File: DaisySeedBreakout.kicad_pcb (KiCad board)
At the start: 2 copper layers, 56.4 x 76.7 mm, 173 parts, among them J10 Conn_01x03, J11 Conn_01x03, J12 Conn_01x03, J13 Conn_01x03, J14 Conn_01x03, J15 Conn_02x08, J16 Conn_01x06, J17 Conn_01x03, J19 Conn_01x03, J2 Conn_02x08, J20 Conn_01x03, J21 Conn_01x03, J22 Conn_01x03, J3 Conn_01x06, J36 MJ-3523-SMT-TR, J37 MJ-3523-SMT-TR, J38 MJ-3523-SMT-TR, J39 MJ-3523-SMT-TR, J4 5027740891, J40 MJ-3523-SMT-TR, J41 MJ-3523-SMT-TR, J42 MJ-3523-SMT-TR, J43 MJ-3523-SMT-TR, J44 MJ-3523-SMT-TR, J45 MJ-3523-SMT-TR, J5 Conn_02x08, J6 Conn_01x03, J7 Conn_01x06, J8 Conn_01x03, J9 Conn_01x03, U1 TCA6424ARGJR, U2 H11L1M, U5 MAX9814

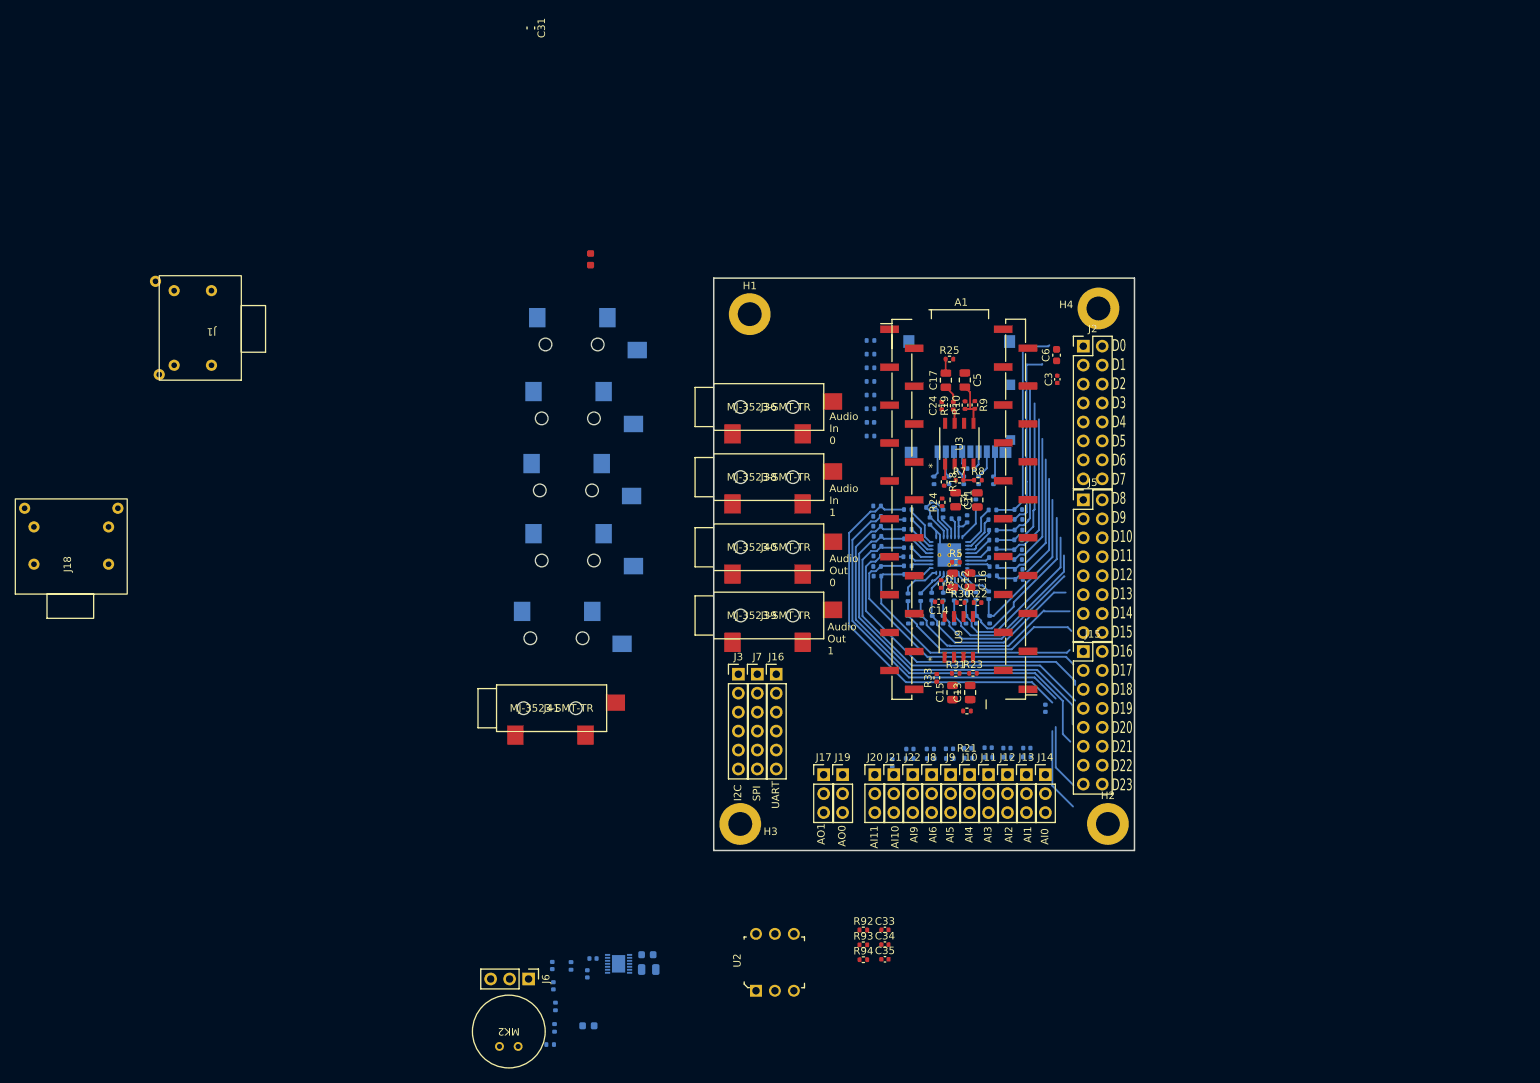
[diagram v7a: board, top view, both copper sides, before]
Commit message: added dual audio back in to prototype that concept
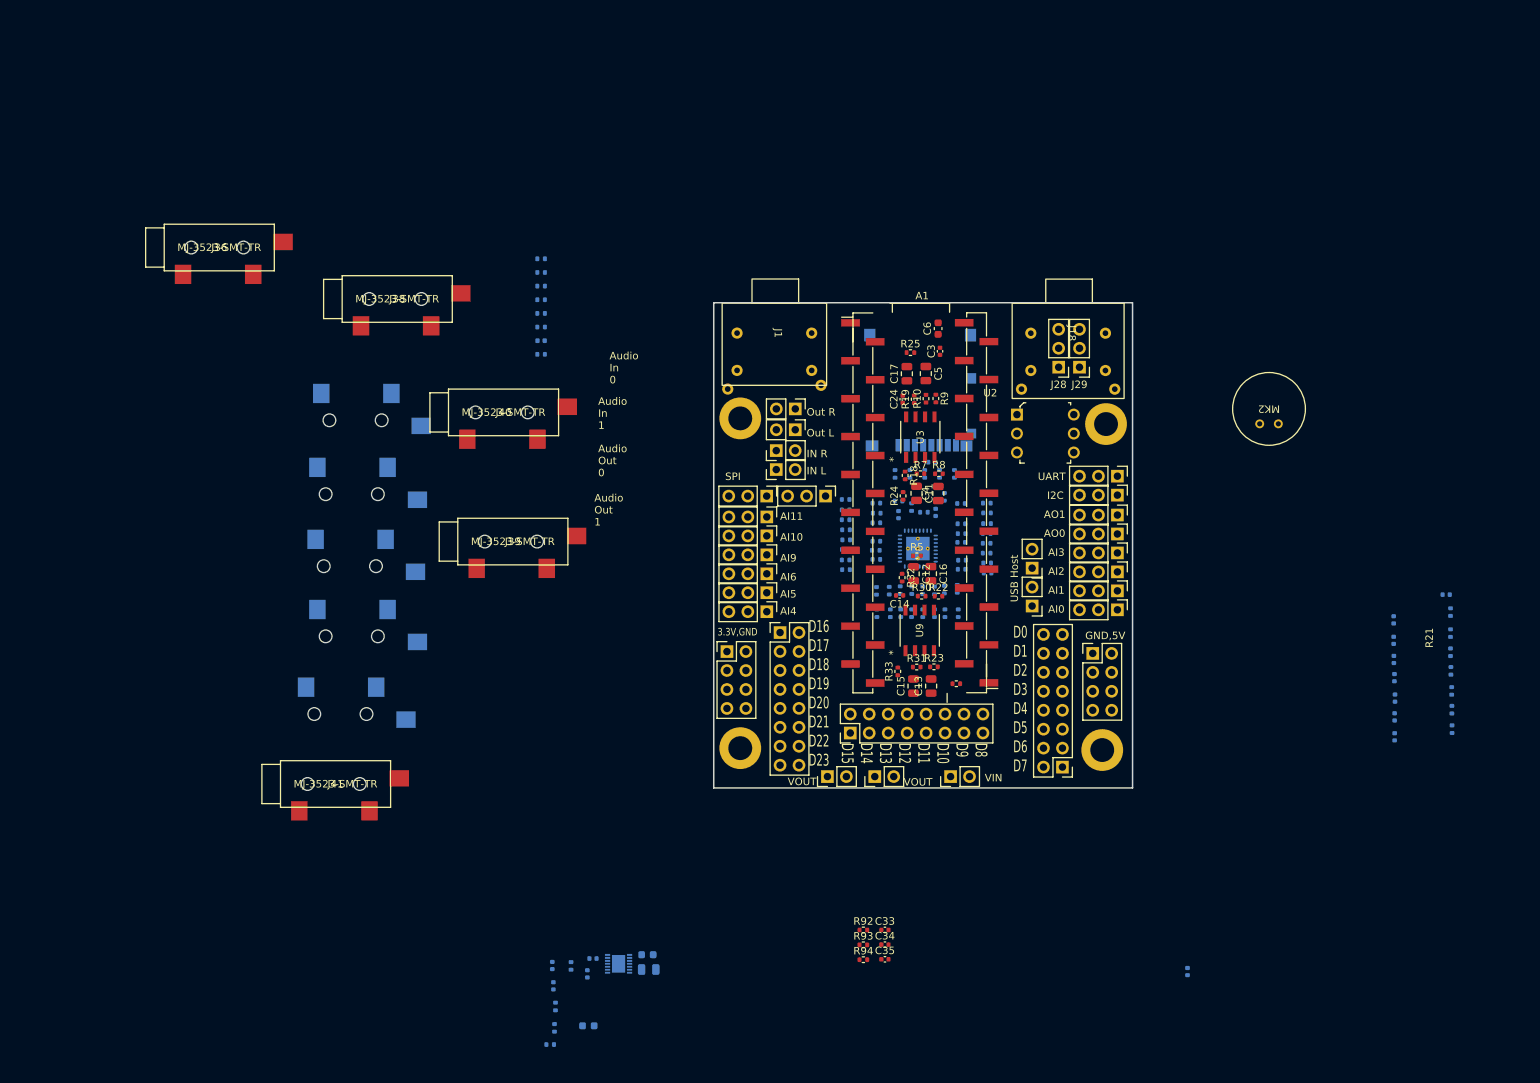
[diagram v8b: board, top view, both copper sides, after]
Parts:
- removed C31: 0.1uF, Capacitor_SMD:C_0603_1608Metric
- added J23: Conn_01x03, Ultralibrarian:PinHeader_1x03_P2.54mm_Vertical_Female, F.Cu at (122.9, 57.9)
- added J24: Conn_01x02, Ultralibrarian:PinHeader_1x02_P2.54mm_Vertical_Female, F.Cu at (118.9, 46.2)
- added J25: Conn_01x02, Ultralibrarian:PinHeader_1x02_P2.54mm_Vertical_Female, F.Cu at (116.3, 54.4)
- added J26: Conn_02x04, Connector_PinHeader_2.54mm:PinHeader_2x04_P2.54mm_Vertical, F.Cu at (158.7, 79.0)
- added J28: Conn_01x03, Ultralibrarian:PinHeader_1x03_P2.54mm_Vertical_Female, F.Cu at (154.2, 40.6)
- added J29: Conn_01x03, Ultralibrarian:PinHeader_1x03_P2.54mm_Vertical_Female, F.Cu at (157.0, 40.6)
- added J30: Conn_01x02, Ultralibrarian:PinHeader_1x02_P2.54mm_Vertical_Female, F.Cu at (116.3, 51.8)
- added J31: Conn_02x04, Connector_PinHeader_2.54mm:PinHeader_2x04_P2.54mm_Vertical, F.Cu at (109.7, 78.8)
- added J32: Conn_01x02, Connector_PinHeader_2.54mm:PinHeader_1x02_P2.54mm_Vertical, F.Cu at (123.2, 95.5)
- added J33: Conn_01x02, Connector_PinHeader_2.54mm:PinHeader_1x02_P2.54mm_Vertical, F.Cu at (129.5, 95.5)
- added J34: Conn_01x02, Connector_PinHeader_2.54mm:PinHeader_1x02_P2.54mm_Vertical, F.Cu at (139.7, 95.5)
- added J35: Conn_01x02, Connector_PinHeader_2.54mm:PinHeader_1x02_P2.54mm_Vertical, F.Cu at (150.6, 67.6)
- added J46: Conn_01x02, Connector_PinHeader_2.54mm:PinHeader_1x02_P2.54mm_Vertical, F.Cu at (150.6, 72.6)
- J16, J3, J7: value Conn_01x06 -> Conn_01x03; footprint Ultralibrarian:PinHeader_1x06_P2.54mm_Vertical_Female -> Ultralibrarian:PinHeader_1x03_P2.54mm_Vertical_Female
- J6: value Conn_01x03 -> Conn_01x02; footprint Connector_PinHeader_2.54mm:PinHeader_1x03_P2.54mm_Vertical -> Ultralibrarian:PinHeader_1x02_P2.54mm_Vertical_Female
- moved J18 137.1 mm to (155.4, 36.1), turned to -90 degrees
- moved MK2 131.7 mm to (182.4, 46.2)
- moved U2 84.8 mm to (148.6, 47.0), turned to 0 degrees
- moved J6 81.8 mm to (118.9, 49.0)
- moved C30 77.6 mm to (206.1, 71.1), turned to 0 degrees
- moved J36 76.7 mm to (41.7, 24.6)
- moved J1 75.4 mm to (116.1, 36.1), turned to -90 degrees
- moved R78 75.1 mm to (206.7, 73.5), turned to -90 degrees
- moved R79 71.7 mm to (206.7, 76.3), turned to -90 degrees
- moved R80 68.6 mm to (206.7, 78.8), turned to -90 degrees
- moved C7 67.1 mm to (199.1, 74.5), turned to -90 degrees
- moved R81 65.7 mm to (206.8, 81.3), turned to -90 degrees
- moved C9 63.8 mm to (199.1, 77.2), turned to -90 degrees
- moved R82 62.7 mm to (206.9, 84.0), turned to -90 degrees
- moved C10 60.8 mm to (199.1, 79.8), turned to -90 degrees
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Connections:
- J6 pad 1: GND -> /Audio Out/AUDIO_OUT_L_EXT
- J6 pad 2: +9V -> GND
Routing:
- net /I2C 24 GPIO/C6: track 59.6 -> 0.00 mm
- net /I2C 24 GPIO/C5: track 55.6 -> 0.00 mm
- net /I2C 24 GPIO/C7: track 53.0 -> 0.00 mm
- net /I2C 24 GPIO/C4: track 51.7 -> 0.00 mm
- net /I2C 24 GPIO/C3: track 47.1 -> 0.00 mm
- net /I2C 24 GPIO/C2: track 44.1 -> 0.00 mm
- net /I2C 24 GPIO/C1: track 39.5 -> 0.00 mm
- net /I2C 24 GPIO/C0: track 35.0 -> 0.00 mm
- net /I2C 24 GPIO/A0: track 28.4 -> 0.00 mm
- net /I2C 24 GPIO/B7: track 27.3 -> 0.00 mm
- net /I2C 24 GPIO/A1: track 26.4 -> 0.00 mm
- net /I2C 24 GPIO/B6: track 25.9 -> 0.00 mm
- net /I2C 24 GPIO/B5: track 24.6 -> 0.00 mm
- net /I2C 24 GPIO/B3: track 23.8 -> 0.00 mm
- net /I2C 24 GPIO/B2: track 23.5 -> 0.00 mm
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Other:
- board size 56.4 x 76.7 mm -> 56.1 x 65 mm
- board text added: "3.3V,GND"
- board text added: "D0 D1 D2 D3 D4 D5 D6 D7"
- board text added: "D16 D17 D18 D19 D20 D21 D22 D23"
- board text added: "D8 D9 D10 D11 D12 D13 D14 D15"
- board text added: "GND,5V"
- board text added: "IN L"
- board text added: "IN R"
- board text added: "Out L"
- board text added: "Out R"
- board text added: "USB Host"
- board text added: "VIN"
- board text added: "VOUT"
- board text removed: "D0 D1 D2 D3 D4 D5 D6 D7 D8 D9 D10 D11 D12 D13 D14 D15 D16 D17 D18 D19 D20 D21 D22 D23"
